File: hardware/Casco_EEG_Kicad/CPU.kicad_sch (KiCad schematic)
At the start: 12 parts, among them J9 FTSH-105-XX-X-DV, SW2 SW_Push, SW3 SW_Push, SW4 SW_Push, U3 LPC845M301JBD64E

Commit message: Primera implementacion de PCB, cambios varios
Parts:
- removed SW2, SW3, SW4: SW_Push, symbol Switch:SW_Push
- removed U3: LPC845M301JBD64E, Huellas:QFP50P1200X1200X160-64N, symbol LPC845:LPC845M301JBD64E
- added S2, S3, S4: SKRPABE010, Huellas:SW_SKRPABE010, symbol SWButton:SKRPABE010
- added U3: LPC845M301JBD48E, Huellas:QFP50P900X900X160-48N, symbol LPC845:LPC845M301JBD48E
- C24: renamed from C16; footprint (none) -> Capacitor_SMD:C_0603_1608Metric
- C25: renamed from C17; footprint (none) -> Capacitor_SMD:C_0603_1608Metric
- R15: renamed from R12; footprint (none) -> Resistor_SMD:R_0603_1608Metric
- R16: renamed from R11; footprint (none) -> Resistor_SMD:R_0603_1608Metric
- R17: renamed from R13; footprint (none) -> Resistor_SMD:R_0603_1608Metric
- R18: renamed from R14; footprint (none) -> Resistor_SMD:R_0603_1608Metric
- R19: renamed from R15; footprint (none) -> Resistor_SMD:R_0603_1608Metric
- renumbered J9 to J11
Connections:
- net +3.3V: now also U3.29 (VDD), U3.32 (VREFP), U3.40 (VDDA)
- net CS/: now also U3.15 (PIO0_16)
- net DRDY/: now also U3.26 (PIO0_8/XTALIN)
- net GNDD: now also S2.1, S2.2, S3.1, S3.2, S4.1, S4.2, U3.30 (VSS), U3.31 (VREFN), U3.41 (VSSA)
- net MISO: now also U3.18 (PIO0_26)
- net MOSI: now also U3.17 (PIO0_27)
- net PIO0_02: now also U3.10 (SWDIO/PIO0_2/TMS)
- net PIO0_03: now also U3.8 (SWDCLK/PIO0_3/TCK)
- net PIO0_04: now also S4.3, S4.4, U3.6 (PIO0_4/ADC_11/TRST/WAKEUP)
- net PIO0_05: now also S2.3, S2.4, U3.5 (PIO0_5/RESET)
- net PIO0_12: now also S3.3, S3.4, U3.4 (PIO0_12)
- net PWDN/: now also U3.37 (PIO0_14/ACMP_I3/ADC_2)
- net RESET: now also U3.25 (PIO0_9/XTALOUT)
- net RX_Master: now also U3.47 (PIO0_18/ADC_8)
- net SCLK: now also U3.44 (PIO0_21/ADC_5)
- net START: now also U3.13 (PIO0_10/I2C0_SCL)
- net TX_Master: now also U3.48 (PIO0_17/ADC_9/DACOUT_0)
- net User_Button: now also U3.45 (PIO0_20/ADC_6)
- new net OnOff_LED: U3.46 (PIO0_19/ADC_7)
- no-connect marks 3 -> 28

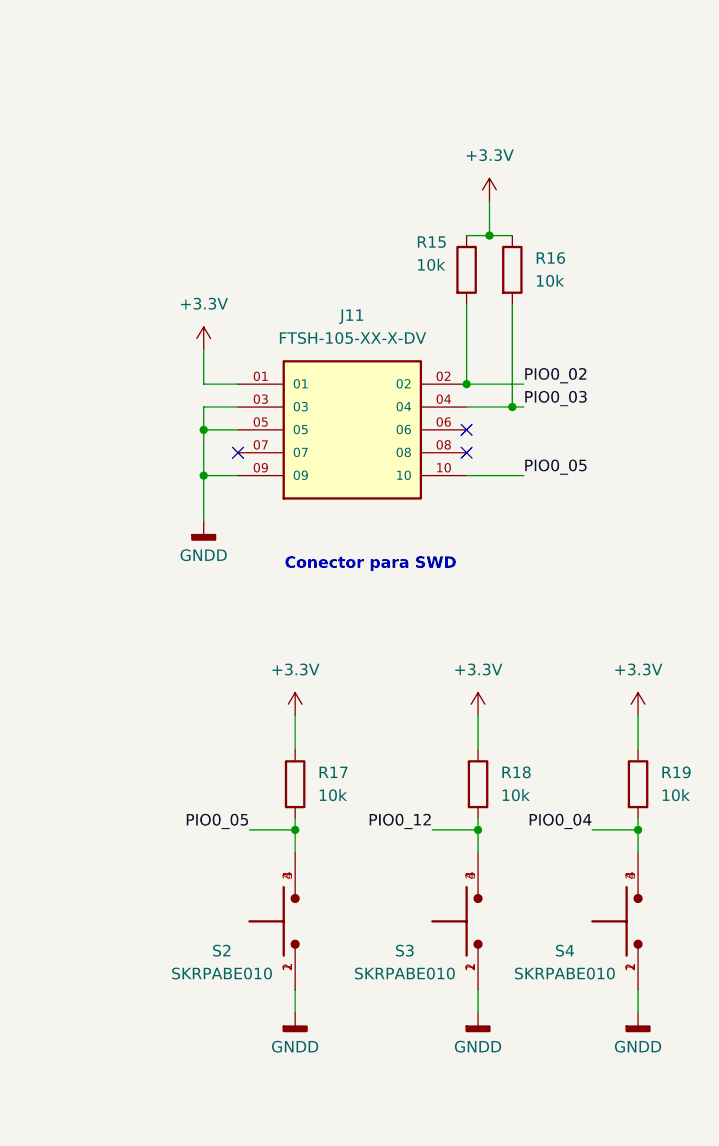
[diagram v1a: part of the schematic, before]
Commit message: Nuevos cambios al PCB, mejoro planos, regulo 3,3V desde 5V, etc
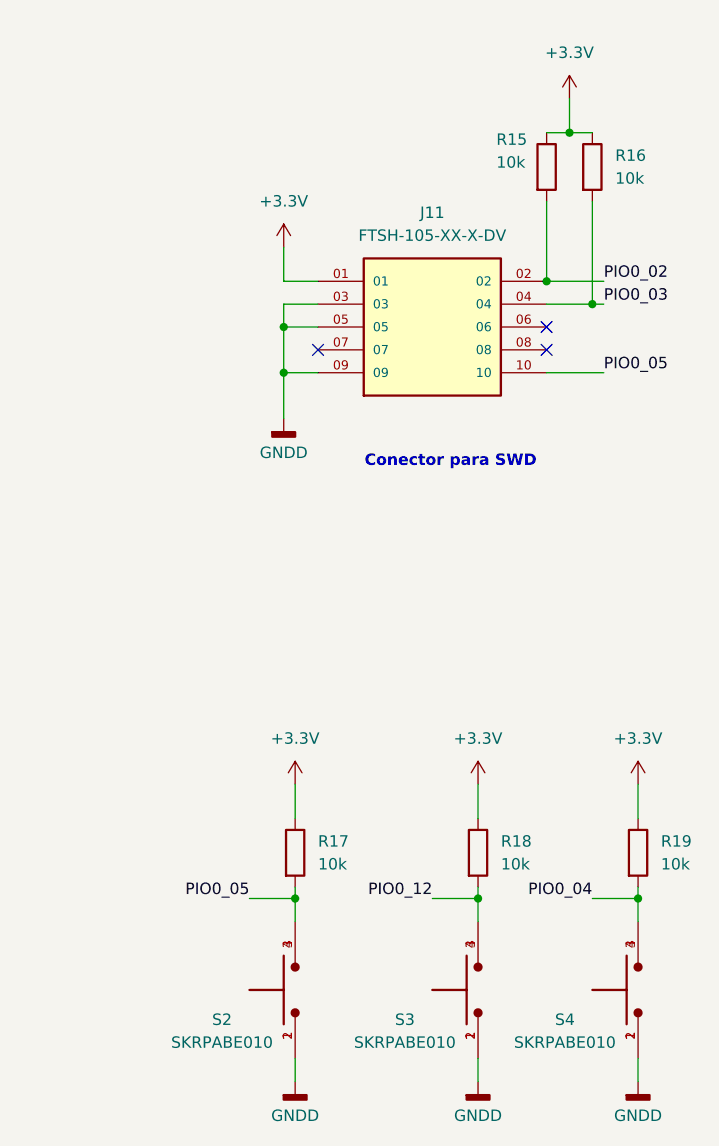
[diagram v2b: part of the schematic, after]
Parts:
- C24: LCSC PN (none) -> C48579280
- C25: LCSC PN (none) -> C57112
- J11: LCSC PN (none) -> C448647
- R15, R16, R17, R18, R19: LCSC PN (none) -> C25804
- S2, S3, S4: LCSC PN (none) -> C115360
- U3: LCSC PN (none) -> C178288
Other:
- moved on the sheet: J11, R15, R16, R17, R18, R19, S2, S3, S4

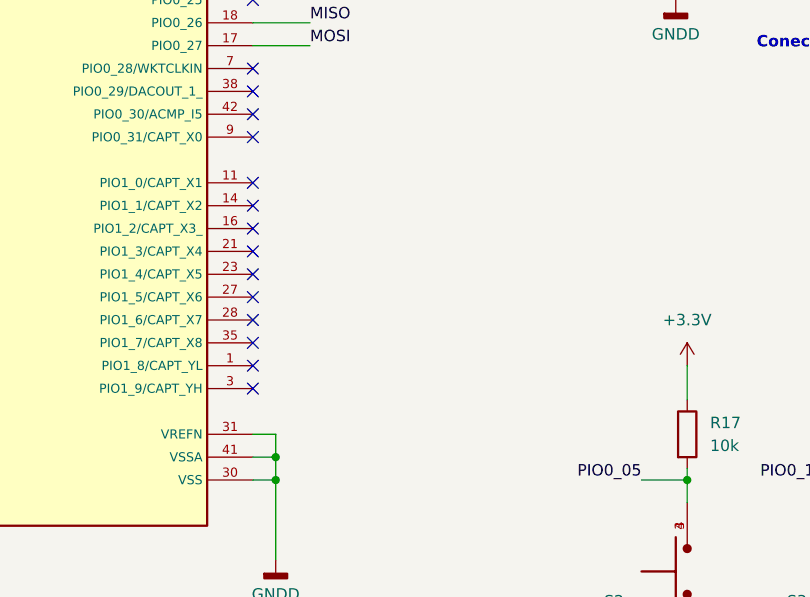
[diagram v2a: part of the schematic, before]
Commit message: Implemento pines I/O para trigger
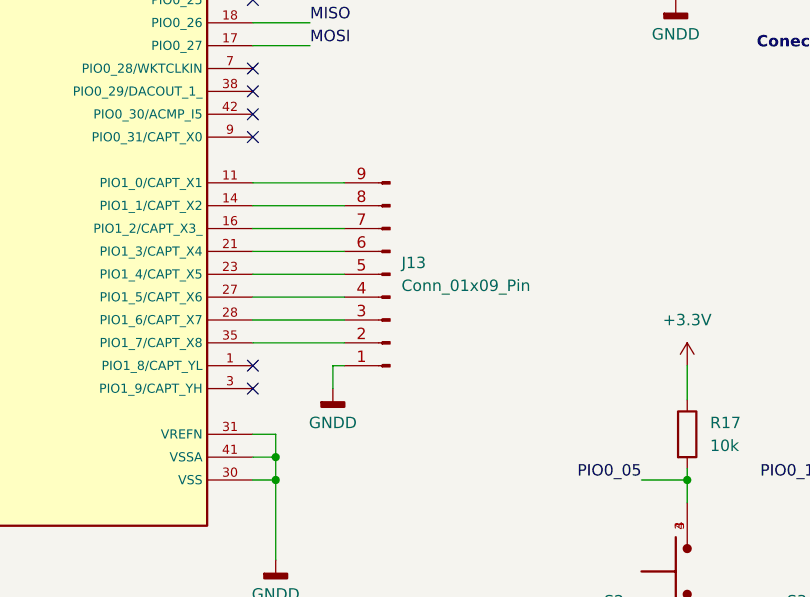
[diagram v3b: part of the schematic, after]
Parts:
- added J13: Conn_01x09_Pin, Connector_PinHeader_2.54mm:PinHeader_1x09_P2.54mm_Horizontal, symbol Connector:Conn_01x09_Pin
- C24: LCSC PN C48579280 -> C14663
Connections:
- net GNDD: now also J13.1 (Pin_1)
- net at U3.11 (PIO1_0/CAPT_X1): now also J13.9 (Pin_9)
- net at U3.14 (PIO1_1/CAPT_X2): now also J13.8 (Pin_8)
- net at U3.16 (PIO1_2/CAPT_X3_): now also J13.7 (Pin_7)
- net at U3.21 (PIO1_3/CAPT_X4): now also J13.6 (Pin_6)
- net at U3.23 (PIO1_4/CAPT_X5): now also J13.5 (Pin_5)
- net at U3.27 (PIO1_5/CAPT_X6): now also J13.4 (Pin_4)
- net at U3.28 (PIO1_6/CAPT_X7): now also J13.3 (Pin_3)
- net at U3.35 (PIO1_7/CAPT_X8): now also J13.2 (Pin_2)
- no-connect marks 28 -> 20

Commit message: Actualización de pcb con aislamiento dc/dc, elimino entradas de trigger
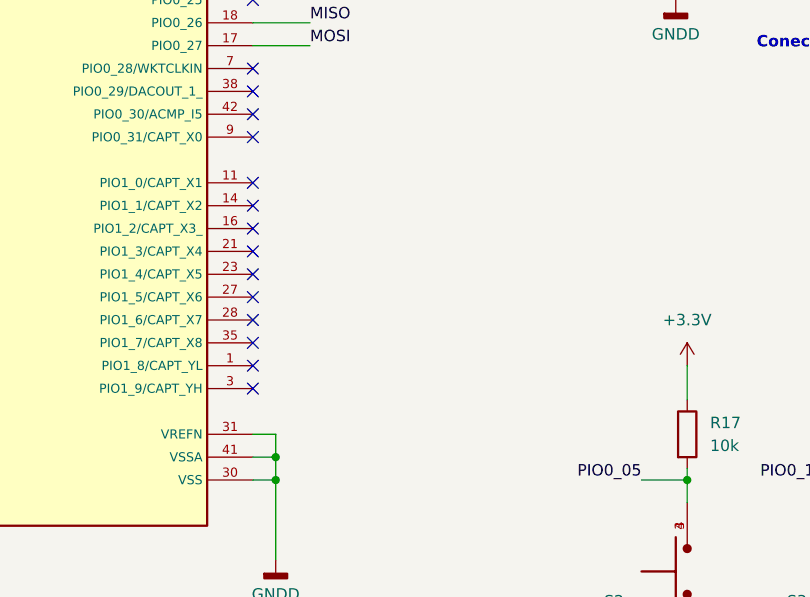
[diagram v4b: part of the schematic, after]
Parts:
- removed J13: Conn_01x09_Pin, Connector_PinHeader_2.54mm:PinHeader_1x09_P2.54mm_Horizontal, symbol Connector:Conn_01x09_Pin
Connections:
- no-connect marks 20 -> 28
